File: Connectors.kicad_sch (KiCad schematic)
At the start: 51 parts, among them J10 0532617010, J12 Conn_01x04, J13 Conn_01x08, J14 1-84952-5, J15 Conn_01x04, J16 Conn_01x03, J17 Conn_01x04, J18 Conn_01x06, J19 Conn_01x04, J20 Conn_01x10, J21 Conn_01x04, J22 Conn_01x04, J23 Conn_01x04, J25 Conn_01x04, J26 Conn_01x03, J28 Conn_01x14, J33 Conn_01x04, J34 Conn_01x04, J7 Conn_01x04, J8 1-84952-5, J9 Conn_01x04, U1 HX0068ANLT, U2 HX0068ANLT, U9 LT3469

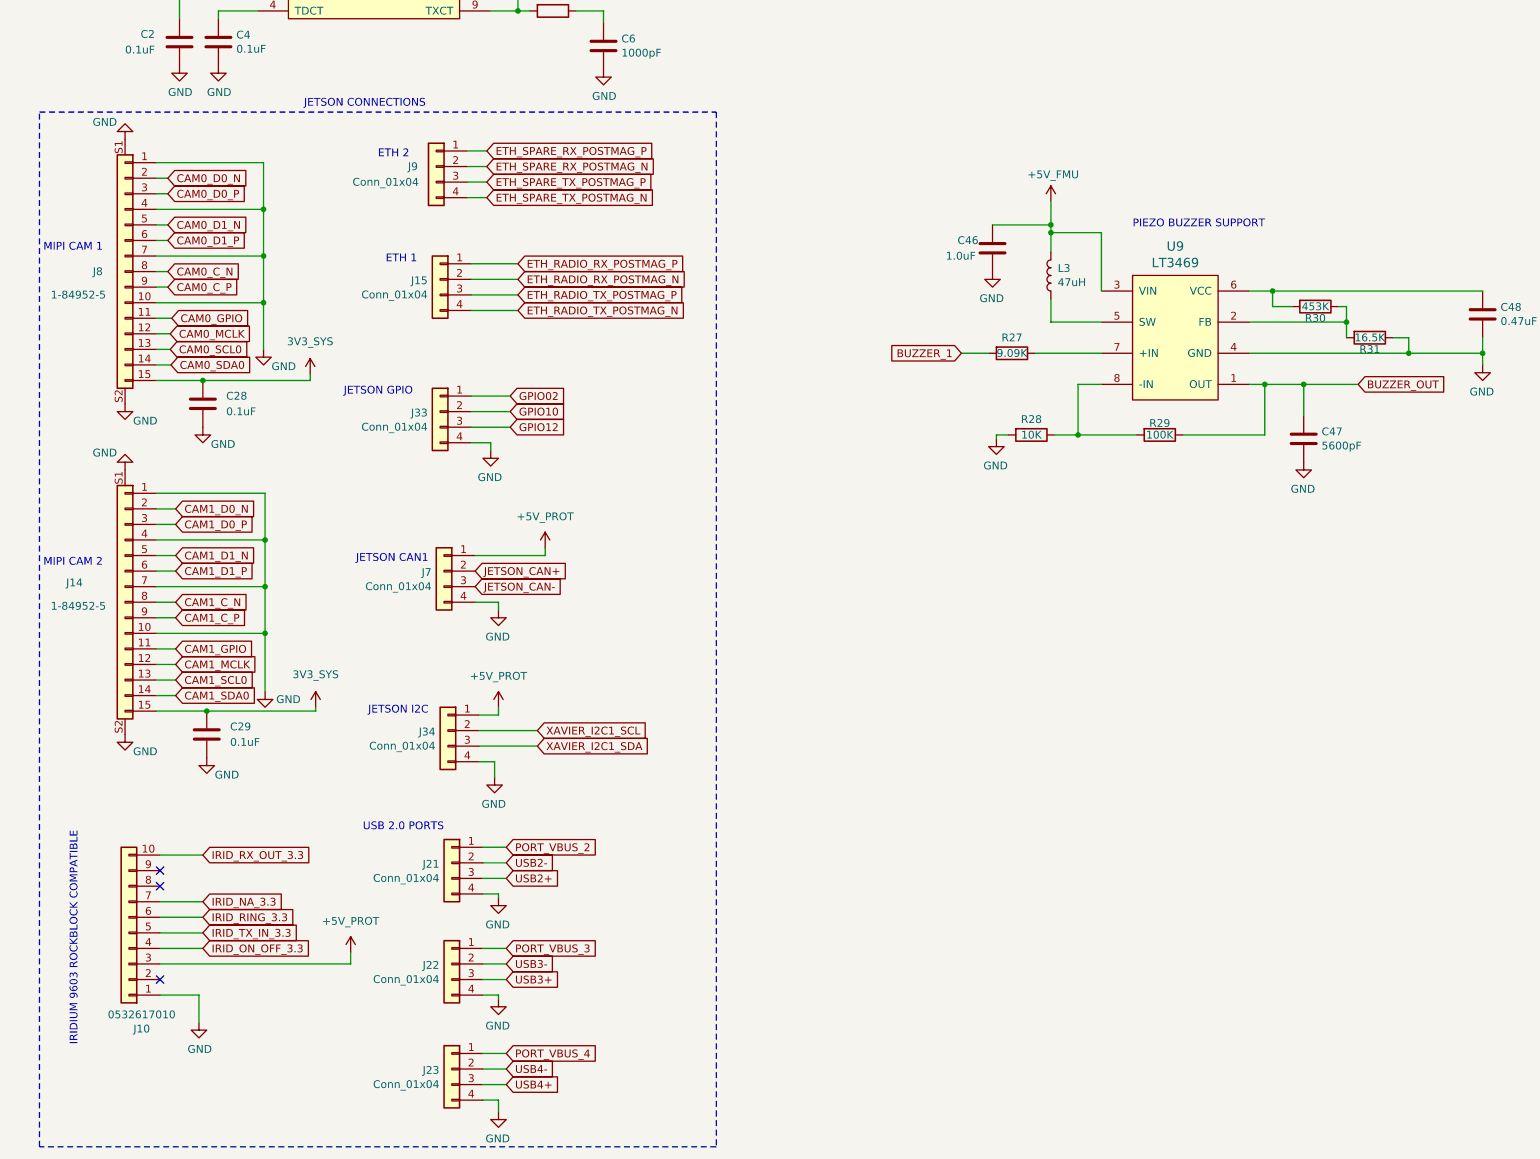
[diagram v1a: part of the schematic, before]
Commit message: updates for Rev1B boards, pinout changes on J5 and J8
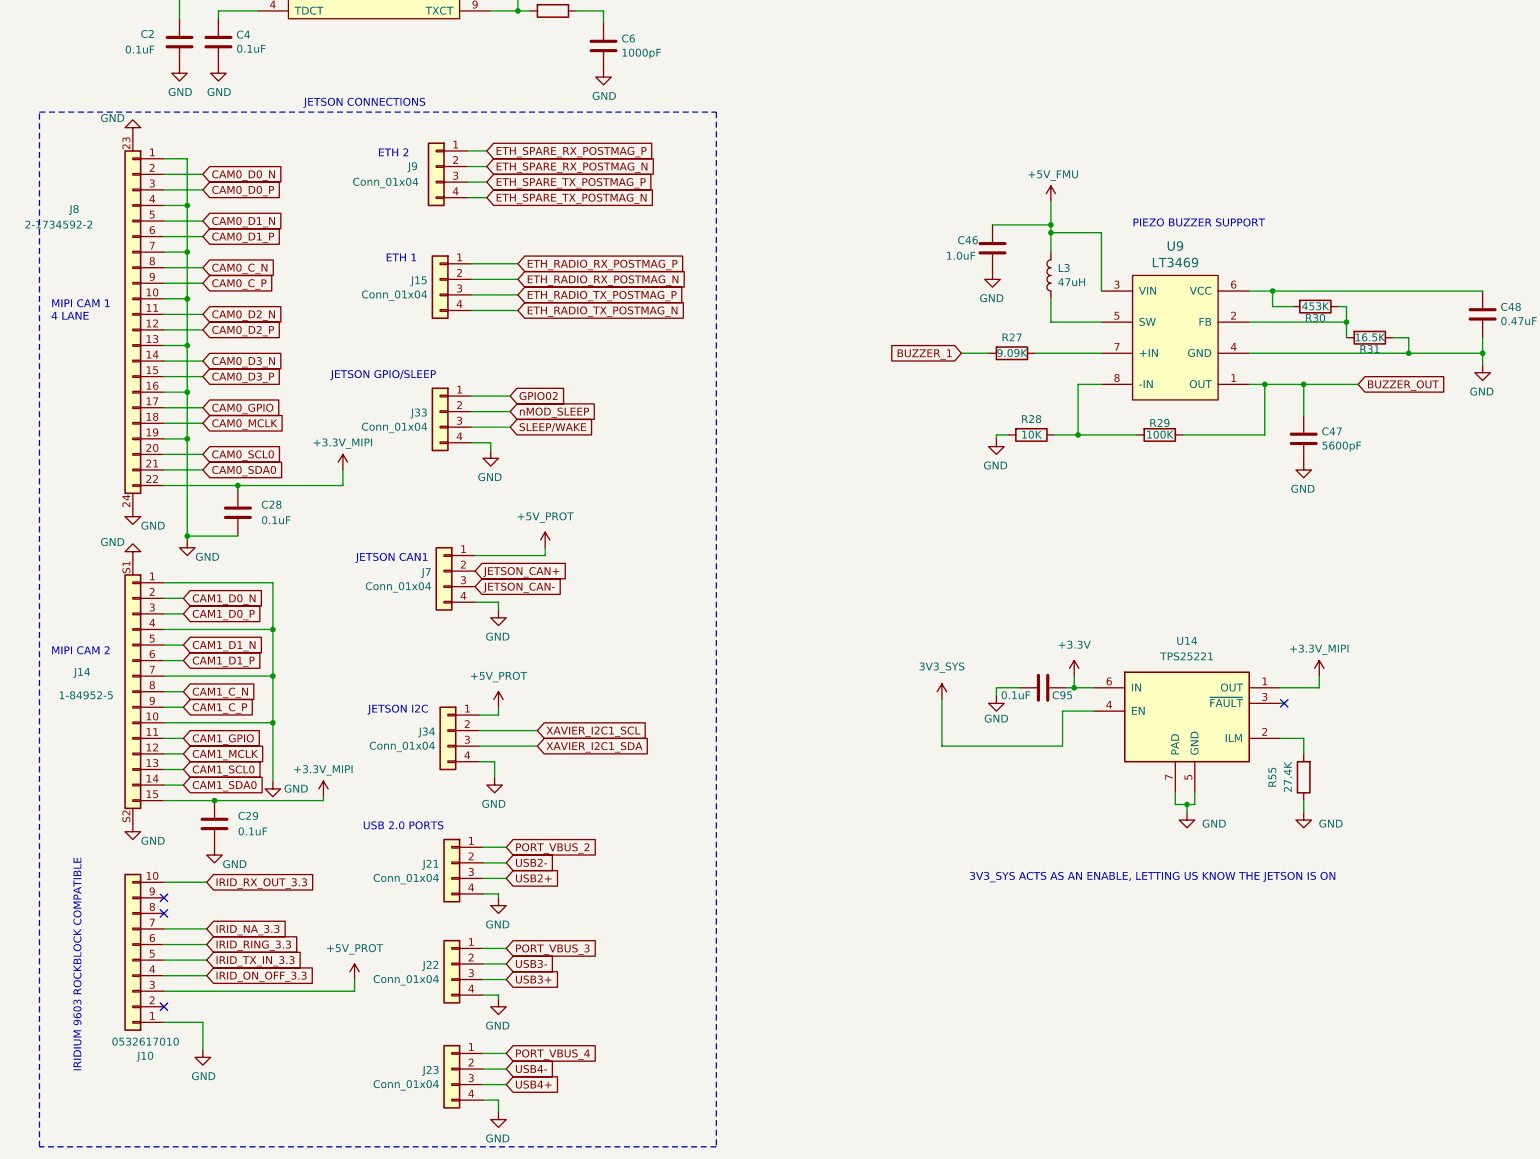
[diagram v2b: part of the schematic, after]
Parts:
- removed J8: 1-84952-5, UVDL:TE_1-84952-5, symbol Connector_Generic:Conn_01x15
- added C95: 0.1uF, Capacitor_SMD:C_0201_0603Metric, symbol Device:C
- added J8: 2-1734592-2, UVDL:CONN22_2-1734592-2, symbol Connector_Generic:Conn_01x22
- added R55: 27.4K, Resistor_SMD:R_0201_0603Metric, symbol Device:R
- added U14: TPS25221, UVDL:DRV0006A, symbol uvdl:TPS25221
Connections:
- net 3V3_SYS: now also U14.4 (EN); no longer C28.1, C29.1, J14.15 (Pin_15)
- net CAM0_C_N: now also J8.8 (Pin_8)
- net CAM0_C_P: now also J8.9 (Pin_9)
- net CAM0_D0_N: now also J8.2 (Pin_2)
- net CAM0_D0_P: now also J8.3 (Pin_3)
- net CAM0_D1_N: now also J8.5 (Pin_5)
- net CAM0_D1_P: now also J8.6 (Pin_6)
- net CAM0_GPIO: now also J8.17 (Pin_17)
- net CAM0_MCLK: now also J8.18 (Pin_18)
- net CAM0_SCL0: now also J8.20 (Pin_20)
- net CAM0_SDA0: now also J8.21 (Pin_21)
- net GND: now also C95.2, J8.1 (Pin_1), J8.10 (Pin_10), J8.13 (Pin_13), J8.16 (Pin_16), J8.19 (Pin_19), J8.23 (S1), J8.24 (S2), J8.4 (Pin_4), J8.7 (Pin_7), R55.1, U14.5 (GND), U14.7 (PAD)
- net GPIO10 renamed nMOD_SLEEP
- net GPIO12 renamed SLEEP/WAKE
- new net: R55.2, U14.2 (ILM)
- new net +3V3: C95.1, U14.6 (IN)
- new net +3V3_MIPI: C28.1, C29.1, J14.15 (Pin_15), J8.22 (Pin_22), U14.1 (OUT)
- new net CAM0_D2_N: J8.11 (Pin_11)
- new net CAM0_D2_P: J8.12 (Pin_12)
- new net CAM0_D3_N: J8.14 (Pin_14)
- new net CAM0_D3_P: J8.15 (Pin_15)
- no-connect marks 3 -> 4
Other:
- note added: "3V3_SYS ACTS AS AN ENABLE, LETTING US KNOW THE JETSON IS ON"
- note added: "JETSON GPIO/SLEEP"
- note added: "MIPI CAM 1 4 LANE"
- note removed: "JETSON GPIO"
- note removed: "MIPI CAM 1"
- moved on the sheet: C28, C29, J10, J14
